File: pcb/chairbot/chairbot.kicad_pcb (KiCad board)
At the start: 2 copper layers, 66.9 x 100 mm, 27 parts, among them J1 Conn_01x02, J2 Conn_01x05, J3 Conn_01x02, J4 Conn_01x07, J5 Conn_01x07, J6 GND, Q1 ZXMN4A06G, U1 ESP32mini, U3 74HCT244, U4 buck-converter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

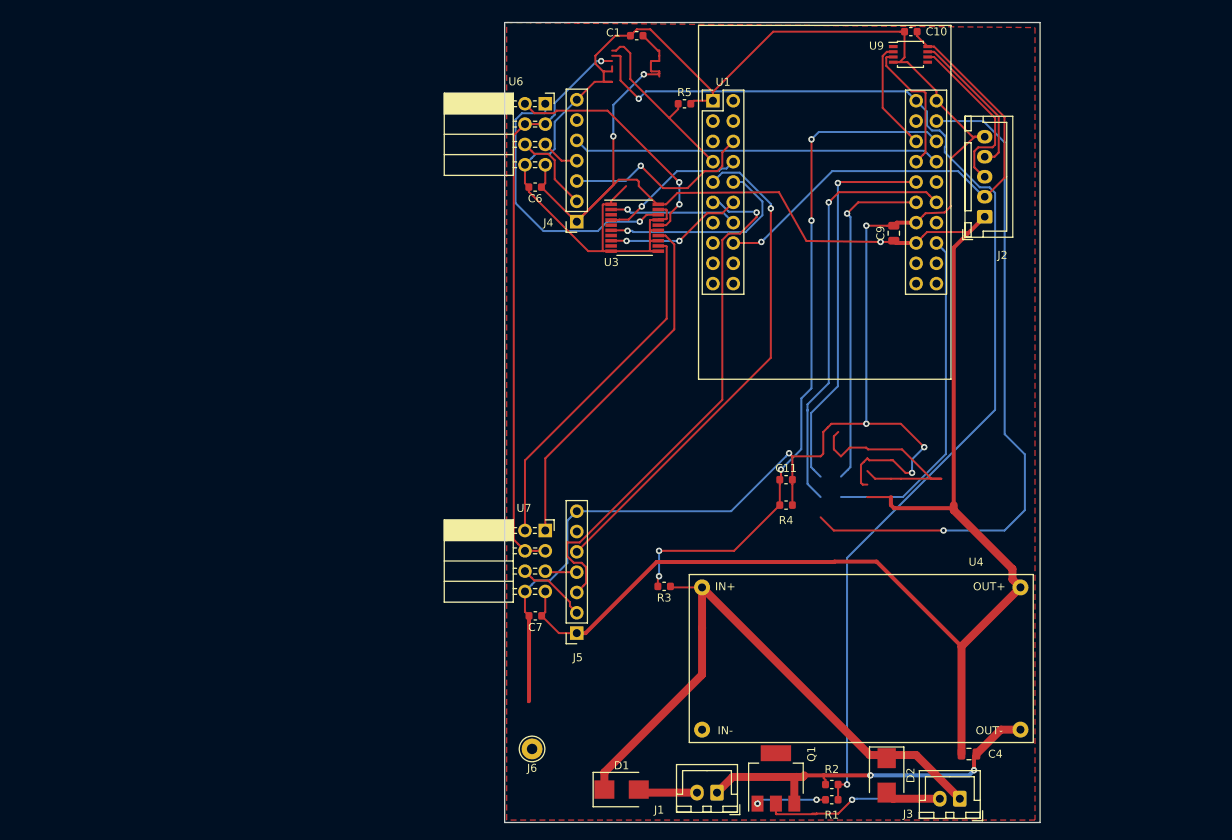
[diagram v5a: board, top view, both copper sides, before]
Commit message: Complete overall schematic.
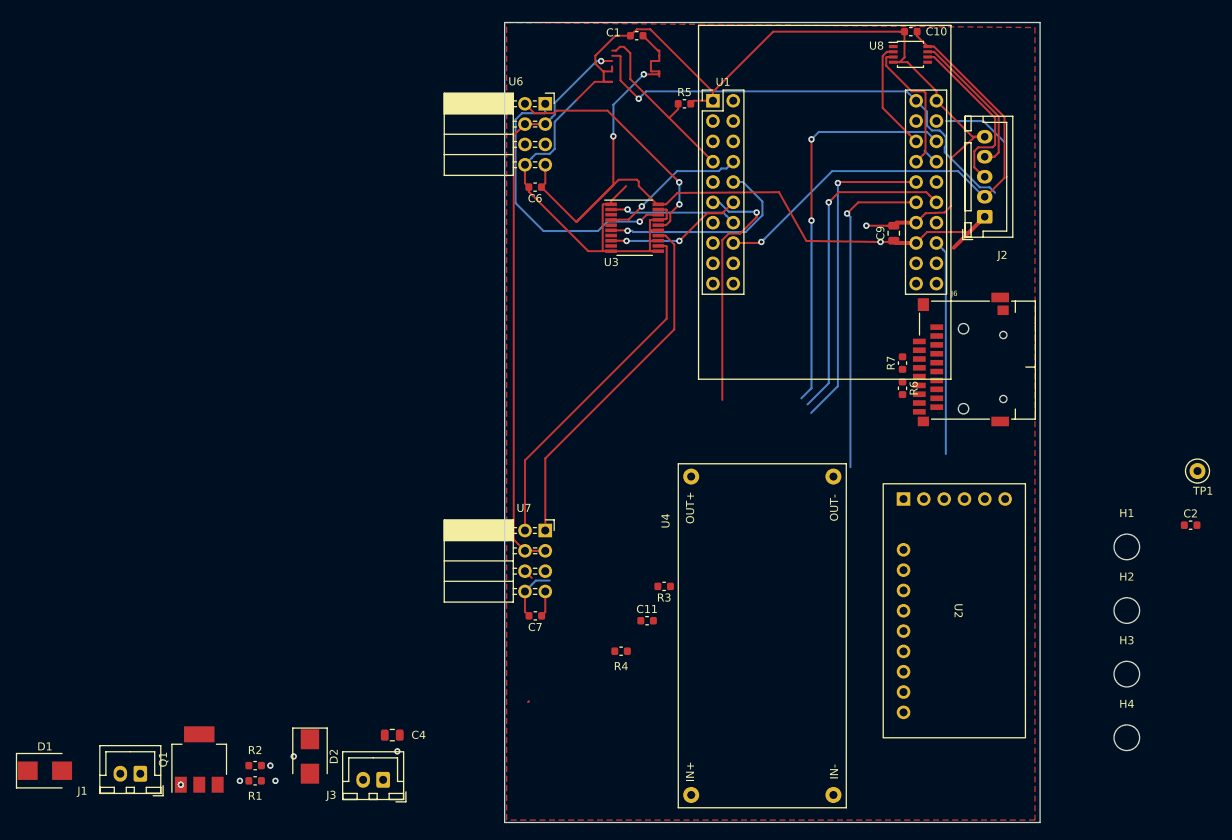
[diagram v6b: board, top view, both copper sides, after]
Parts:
- removed J4, J5: Conn_01x07, chairbot:peakdetector
- added C2: 100n, Capacitor_SMD:C_0603_1608Metric, F.Cu at (122.3, 143.5)
- added H1: MountingHole, MountingHole:MountingHole_3.2mm_M3, F.Cu at (114.3, 146.2)
- added H2: MountingHole, MountingHole:MountingHole_3.2mm_M3, F.Cu at (114.3, 154.1)
- added H3: MountingHole, MountingHole:MountingHole_3.2mm_M3, F.Cu at (114.3, 162.1)
- added H4: MountingHole, MountingHole:MountingHole_3.2mm_M3, F.Cu at (114.3, 170.0)
- added R6: 10k, Resistor_SMD:R_0603_1608Metric, F.Cu at (86.3, 126.4)
- added R7: 10k, Resistor_SMD:R_0603_1608Metric, F.Cu at (86.3, 123.2)
- added TP1: GND, TestPoint:TestPoint_Loop_D1.80mm_Drill1.0mm_Beaded, F.Cu at (123.2, 136.7)
- added U2: PCM5102A module, Custom:PCM5102A module, F.Cu at (92.8, 154.2)
- J6: value GND -> Micro_SD_Card_Det1; footprint Connector_Pin:Pin_D1.3mm_L11.0mm -> Custom:J_SD_Card-micro_dual
- Q1: footprint Package_TO_SOT_SMD:SOT-223 -> Package_TO_SOT_SMD:SOT-223-3_TabPin2
- moved J6 73.1 mm to (95.4, 123.7), turned to -90 degrees
- moved D1 72.1 mm to (-20.9, 174.2)
- moved D2 72.1 mm to (12.2, 172.4)
- moved J1 72.1 mm to (-8.97, 174.5)
- moved Q1 72.1 mm to (-1.60, 172.8)
- moved R1 72.1 mm to (5.38, 175.4)
- moved R2 72.1 mm to (5.38, 173.5)
- moved C4 72.1 mm to (22.5, 169.7)
- moved J3 72.1 mm to (21.4, 175.3)
- moved R4 27.5 mm to (51.1, 159.2)
- moved C11 24.8 mm to (54.4, 155.4)
- moved U4 12.7 mm to (68.8, 157.3), turned to 90 degrees
- renumbered U9 to U8
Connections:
- J6 pad 1: GND -> Net-(J6-DAT2)
- U1 pad 11: IS_B_L_P -> unconnected-(U1-IO34-Pad11)
- U1 pad 24: MISO -> MOSI
- U1 pad 28: IS_A_R_P -> SCK
- U1 pad 29: CE -> unconnected-(U1-IO17-Pad29)
- U1 pad 30: (no net) -> unconnected-(U1-TDI-Pad30)
- U1 pad 31: CS -> unconnected-(U1-IO16-Pad31)
- U1 pad 32: SCK -> unconnected-(U1-IO4-Pad32)
- U1 pad 36: MOSI -> unconnected-(U1-IO2-Pad36)
- U1 pad 6: IS_A_L_P -> CS
- U1 pad 9: IS_B_R_P -> MISO
- U6 pad 5: IS_A_R -> unconnected-(U6-R_IS-Pad5)
- U6 pad 6: IS_A_L -> unconnected-(U6-L_IS-Pad6)
- U7 pad 5: IS_B_R -> unconnected-(U7-R_IS-Pad5)
- U7 pad 6: IS_B_L -> unconnected-(U7-L_IS-Pad6)
- U8 pad 1: (no net) -> unconnected-(U8-NC-Pad1)
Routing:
- net GND: track 332.5 -> 168.0 mm, vias 7 -> 3
- net +5V: track 253.9 -> 110.3 mm
- net EN: track 167.4 -> 72.3 mm, vias 2 -> 3
- net Vbat: track 85.8 -> 0.00 mm, vias 5 -> 0
- net MISO: track 83.9 -> 0.00 mm, vias 1 -> 0
- net +24V: track 77.5 -> 0.00 mm
- net IS_B_L_P: track 67.1 -> 0.00 mm, vias 1 -> 0
- net IS_B_R_P: track 62.9 -> 0.00 mm, vias 1 -> 0
- net unconnected-(U1-U0TXD-Pad21): track 0.00 -> 59.9 mm, vias 0 -> 1
- net SCK: track 53.3 -> 2.06 mm, vias 1 -> 0
- net CE: track 48.4 -> 0.00 mm, vias 1 -> 0
- net IS_A_R_P: track 46.1 -> 0.00 mm
- net CS: track 42.8 -> 0.00 mm, vias 1 -> 0
- net unconnected-(U1-IO16-Pad31): track 0.00 -> 41.1 mm, vias 0 -> 1
- net unconnected-(U1-IO4-Pad32): track 0.00 -> 40.9 mm, vias 0 -> 1
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
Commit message: Fix errors.
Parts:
- moved H1 95.7 mm to (41.0, 84.7)
- moved D1 95.5 mm to (74.4, 167.3), turned to -90 degrees
- moved J1 86.5 mm to (77.5, 176.5)
- moved H3 78.9 mm to (98.6, 84.7)
- moved H2 76.6 mm to (41.0, 176.1)
- moved C4 74.5 mm to (77.2, 119.1)
- moved TP1 52.6 mm to (87.8, 175.6)
- moved R1 45.7 mm to (48.3, 159.7), turned to -90 degrees
- moved Q1 45.0 mm to (41.8, 160.6)
- moved R2 44.1 mm to (48.3, 163.1), turned to 90 degrees
- moved C2 43.3 mm to (83.2, 124.9), turned to -90 degrees
- moved D2 35.5 mm to (47.6, 169.2)
- moved R5 28.5 mm to (85.5, 101.5), turned to -90 degrees
- moved C11 22.4 mm to (76.6, 158.3), turned to 90 degrees
- moved R4 22.0 mm to (73.1, 158.2), turned to 90 degrees
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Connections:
- R1 pad 2: EN -> EN5
- R2 pad 2: EN -> EN5
- U1 pad 24: MOSI -> unconnected-(U1-IO27-Pad24)
- U1 pad 29: unconnected-(U1-IO17-Pad29) -> MISO
- U1 pad 31: unconnected-(U1-IO16-Pad31) -> MOSI
- U1 pad 32: unconnected-(U1-IO4-Pad32) -> CS
- U1 pad 6: CS -> unconnected-(U1-IO26-Pad6)
- U1 pad 9: MISO -> unconnected-(U1-IO33-Pad9)
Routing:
- net +5V: track 110.3 -> 19.5 mm, vias 3 -> 0
- net EN: track 72.3 -> 0.14 mm, vias 3 -> 0
- net unconnected-(U1-U0TXD-Pad21): track 59.9 -> 0.00 mm, vias 1 -> 0
- net GND: track 168.0 -> 112.3 mm, vias 3 -> 0
- net unconnected-(U1-IO16-Pad31): track 41.1 -> 0.00 mm, vias 1 -> 0
- net unconnected-(U1-IO4-Pad32): track 40.9 -> 0.00 mm, vias 1 -> 0
- net unconnected-(U1-IO17-Pad29): track 40.0 -> 0.00 mm, vias 1 -> 0
- net unconnected-(U1-IO2-Pad36): track 26.9 -> 0.00 mm
- net EN5: track 72.1 -> 59.6 mm, vias 1 -> 0
- net +3V3: track 63.2 -> 69.3 mm
- net MOSI: track 8.43 -> 2.36 mm
- net Net-(J6-DAT2): track 0.00 -> 5.73 mm
- net Net-(J6-DAT1): track 0.00 -> 4.93 mm
- net MISO: track 0.00 -> 2.38 mm
- net CS: track 0.00 -> 2.36 mm
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
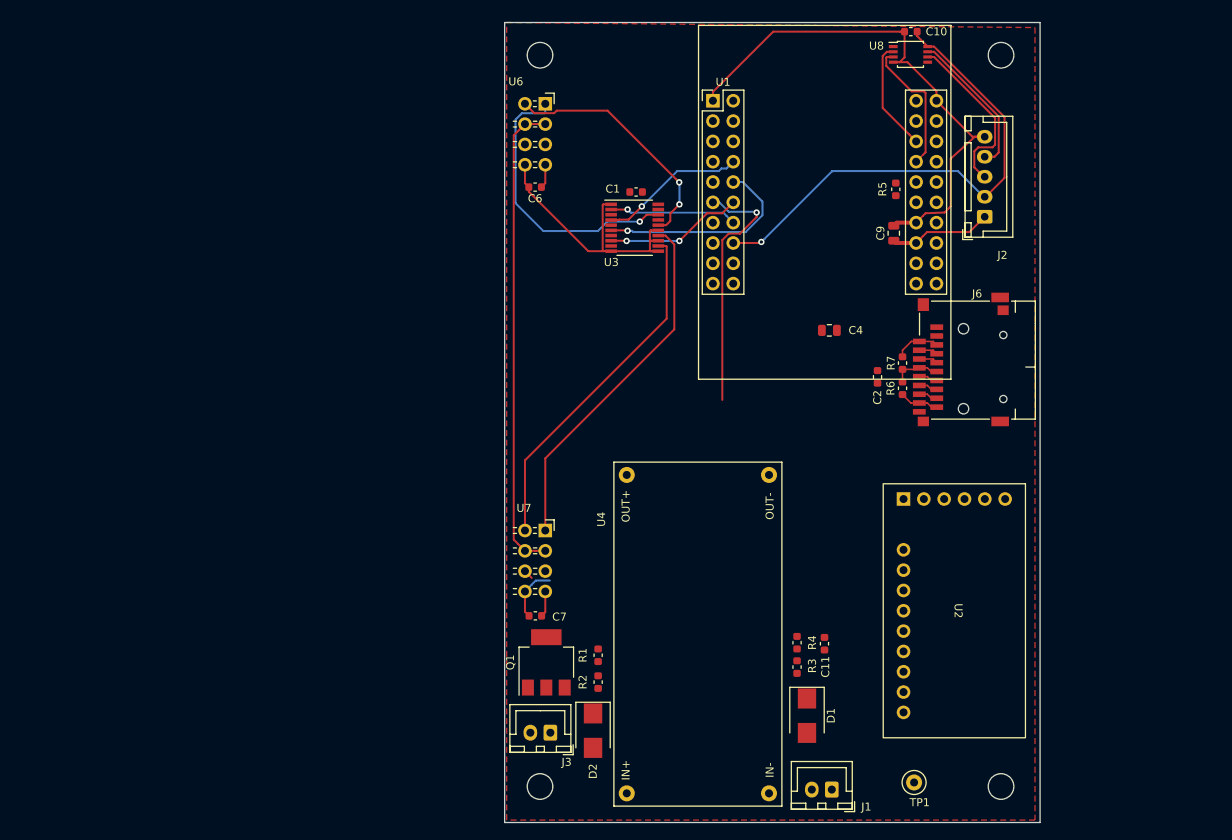
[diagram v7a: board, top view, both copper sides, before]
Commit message: Complete routing.
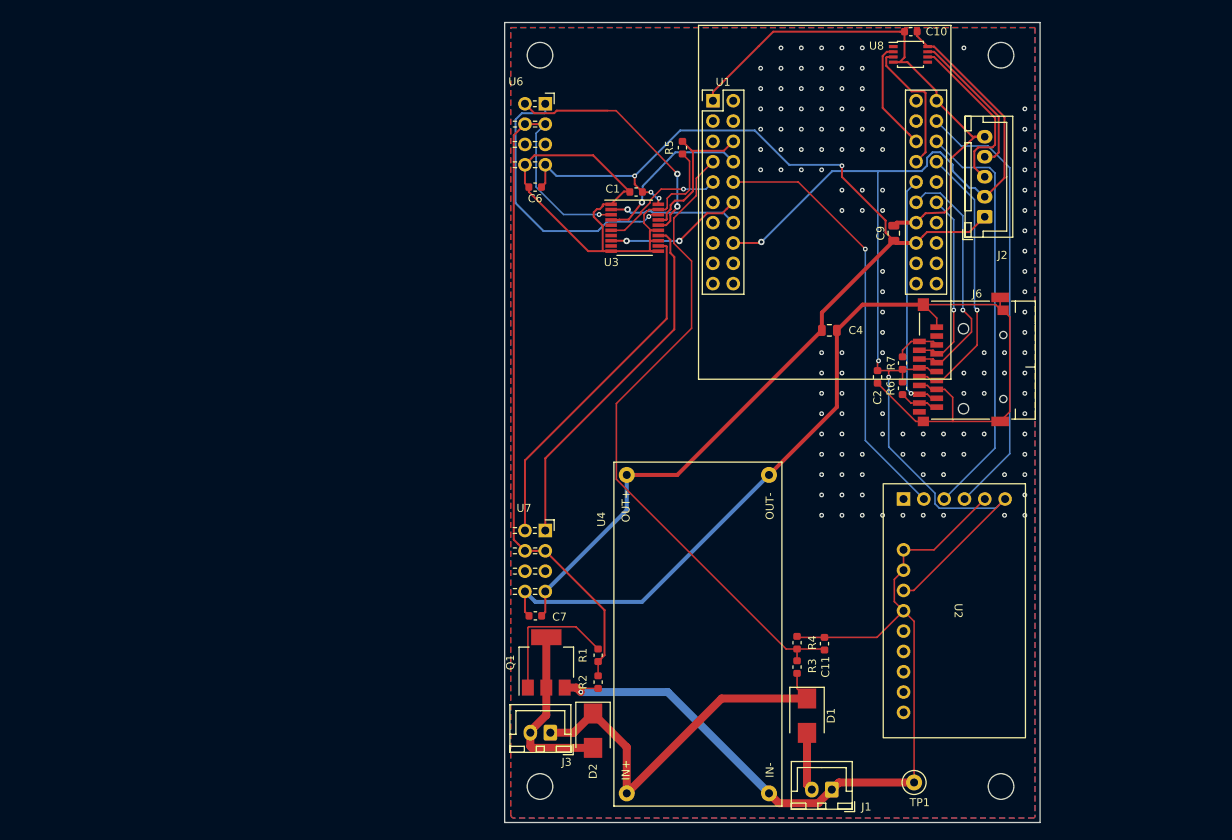
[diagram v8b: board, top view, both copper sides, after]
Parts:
- moved R5 27.2 mm to (58.8, 96.3)
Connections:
- U1 pad 10: IO19 -> BCK
- U1 pad 24: unconnected-(U1-IO27-Pad24) -> SRCK
- U1 pad 26: EN -> DIN
- U1 pad 6: unconnected-(U1-IO26-Pad6) -> EN
- U1 pad 9: unconnected-(U1-IO33-Pad9) -> IO33
- U3 pad 6: IO19 -> IO33
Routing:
- net GND: track 112.3 -> 379.5 mm, vias 0 -> 123
- net +5V: track 19.5 -> 144.6 mm, vias 0 -> 4
- net Vbat: track 0.00 -> 82.9 mm
- net +3V3: track 69.3 -> 146.5 mm, vias 1 -> 3
- net SRCK: track 0.00 -> 55.3 mm
- net BCK: track 0.00 -> 54.3 mm, vias 0 -> 1
- net DIN: track 0.00 -> 52.3 mm
- net +24V: track 0.00 -> 49.2 mm
- net EN5: track 59.6 -> 97.8 mm, vias 0 -> 1
- net unconnected-(U1-IO34-Pad11): track 32.0 -> 0.00 mm, vias 1 -> 0
- net SCK: track 2.37 -> 34.3 mm, vias 0 -> 1
- net MOSI: track 2.36 -> 30.8 mm, vias 0 -> 1
- net MISO: track 2.38 -> 30.6 mm, vias 0 -> 1
- net IO19: track 26.2 -> 0.00 mm, vias 1 -> 0
- net Net-(D2-A): track 0.00 -> 22.4 mm
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- added copper zone on B.Cu, net GND
